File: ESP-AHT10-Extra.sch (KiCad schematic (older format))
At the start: 26 parts, among them J1 USB, SW1 RESET, SW2 PROG, U1 CH330N, U2 HT7233, U3 ESP-12, U4 AHT10, U5 USBLC6-2SC6

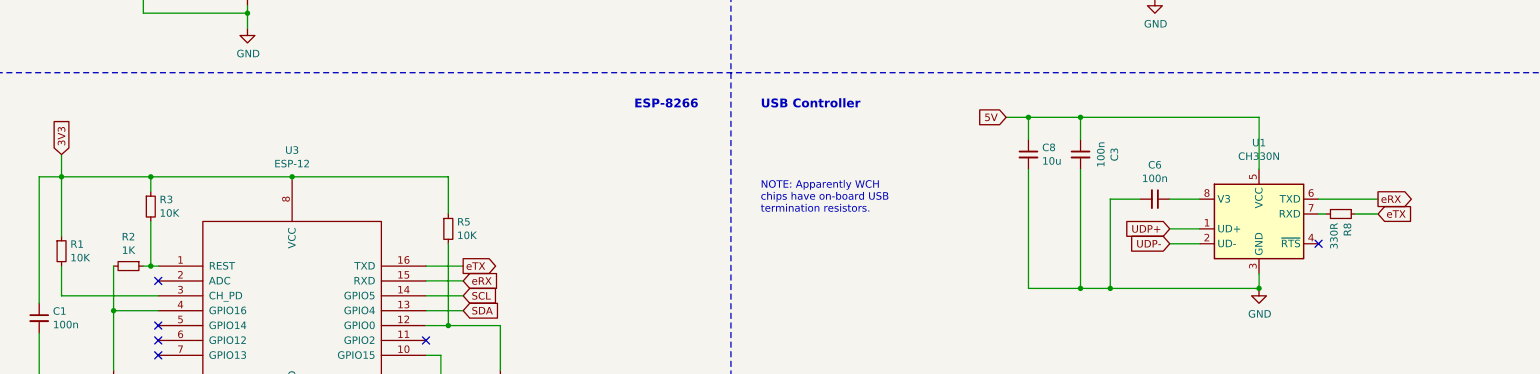
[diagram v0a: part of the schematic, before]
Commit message: really no excuse not to connect RTS to RESET
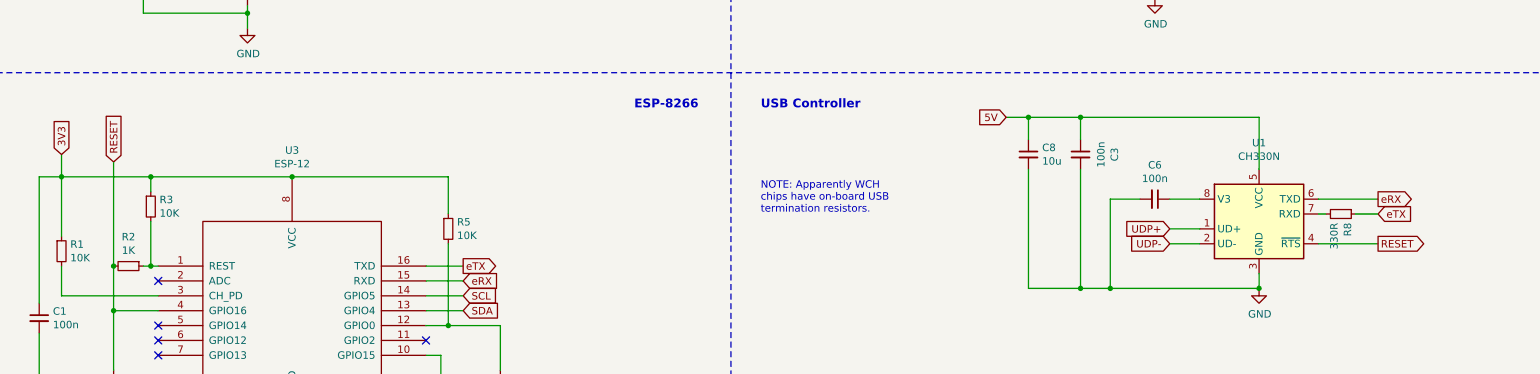
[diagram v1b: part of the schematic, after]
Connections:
- net RESET: now reaches R2.2, SW1.1, U3.4 (GPIO16)
- net RESET: now also U1.4 (~RTS)
- no-connect marks 6 -> 5
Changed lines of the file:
@@
 Wire Wire Line
 	8550 5750 8750 5750
-NoConn ~ 9550 5750
 $Comp
 L power:GND #PWR01
@@
 Text Notes 650  7600 0    50   ~ 0
 NOTE: R3 isn't needed for\nESP modules having an internal\nRESET pull-up. It'll still work if you\nadd it though.
+Text GLabel 1450 5200 1    50   Input ~ 0
+RESET
+Wire Wire Line
+	1450 5200 1450 5900
+Connection ~ 1450 5900
+Text GLabel 9950 5750 2    50   Output ~ 0
+RESET
+Wire Wire Line
+	9550 5750 9950 5750
 $EndSCHEMATC

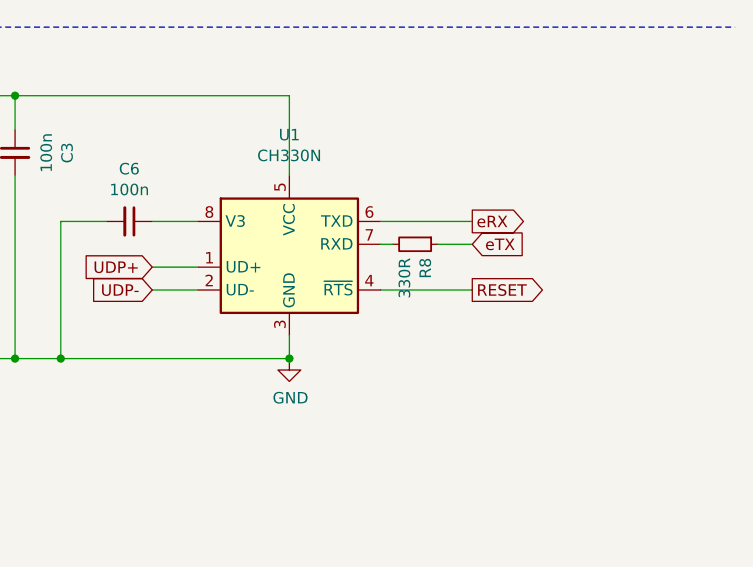
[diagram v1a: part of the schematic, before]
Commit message: fix R8's value
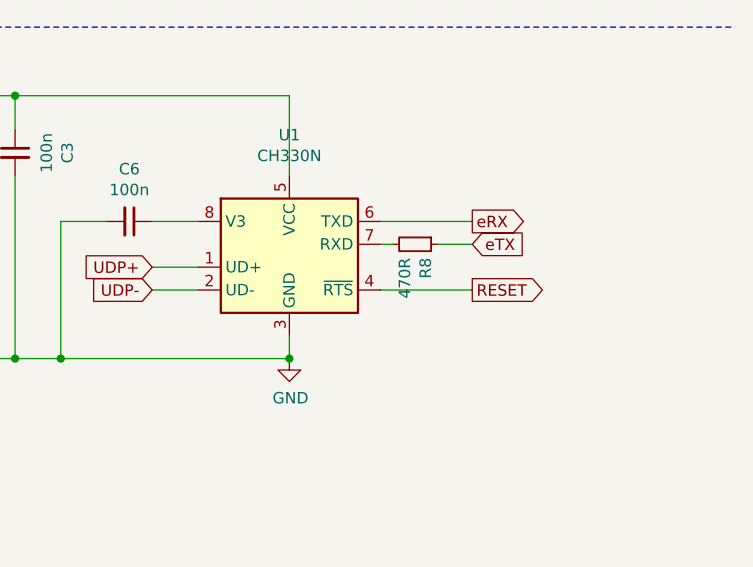
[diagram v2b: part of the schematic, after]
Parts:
- R8: value 330R -> 470R
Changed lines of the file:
@@
 P 9700 5550
 F 0 "R8" H 9759 5596 50  0000 L CNN
-F 1 "330R" H 9759 5505 50  0000 L CNN
+F 1 "470R" H 9759 5505 50  0000 L CNN
 F 2 "Resistors_SMD:R_0805" H 9700 5550 50  0001 C CNN
 F 3 "~" H 9700 5550 50  0001 C CNN

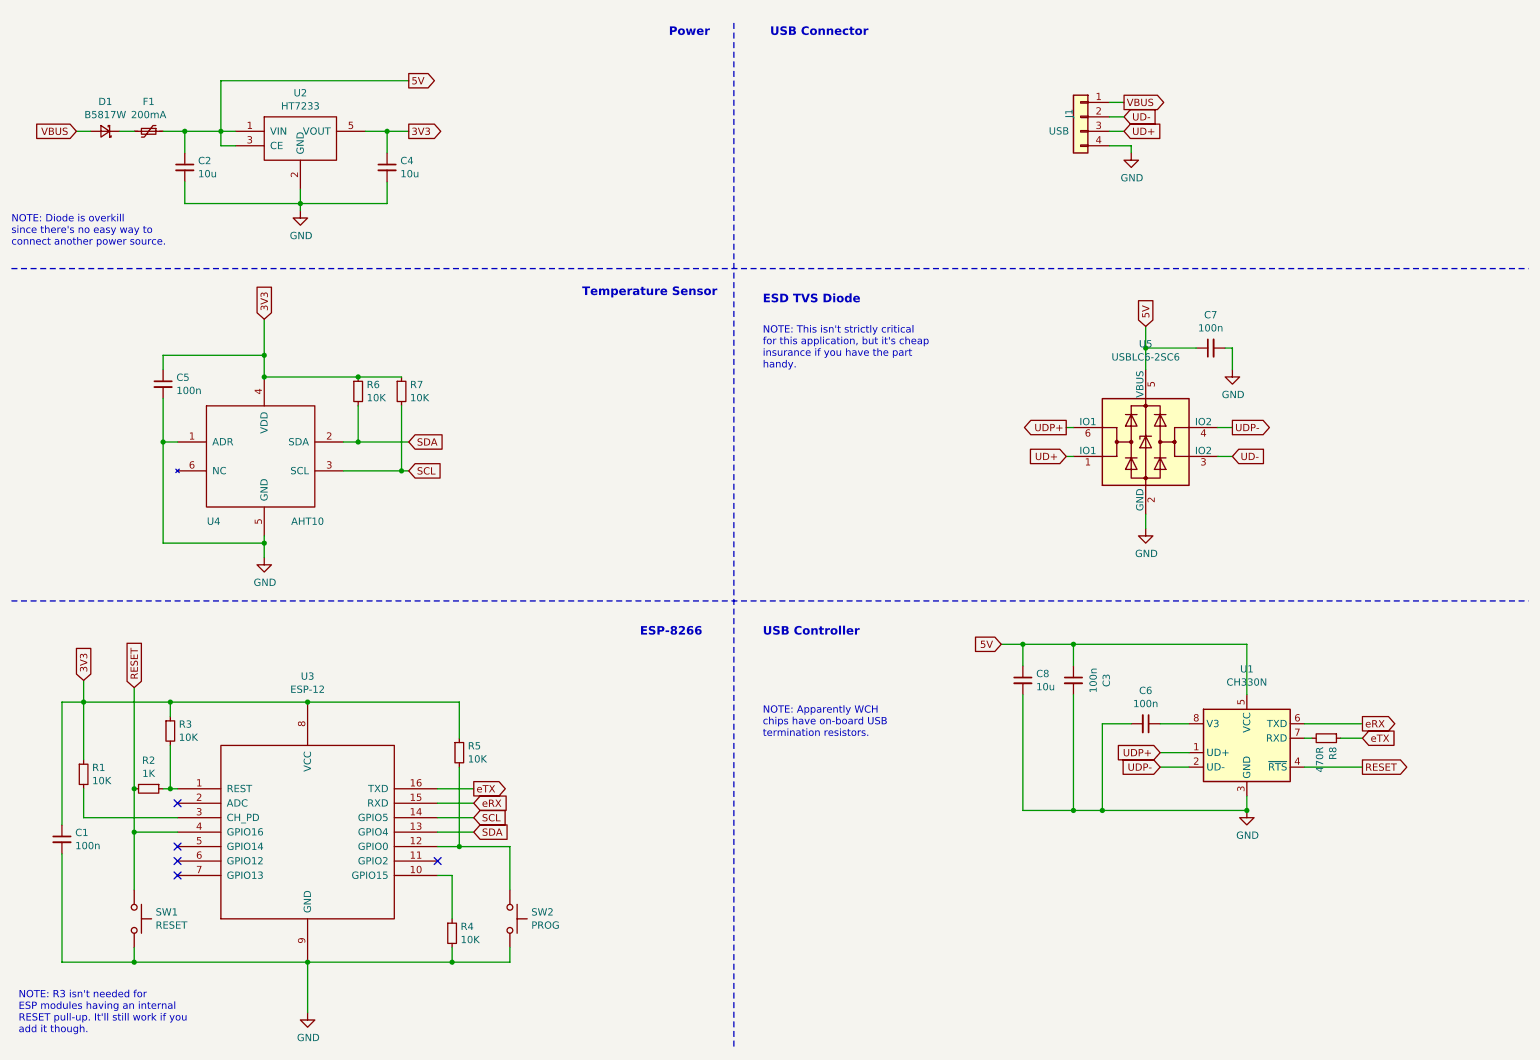
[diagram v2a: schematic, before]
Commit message: try adding a WLED.
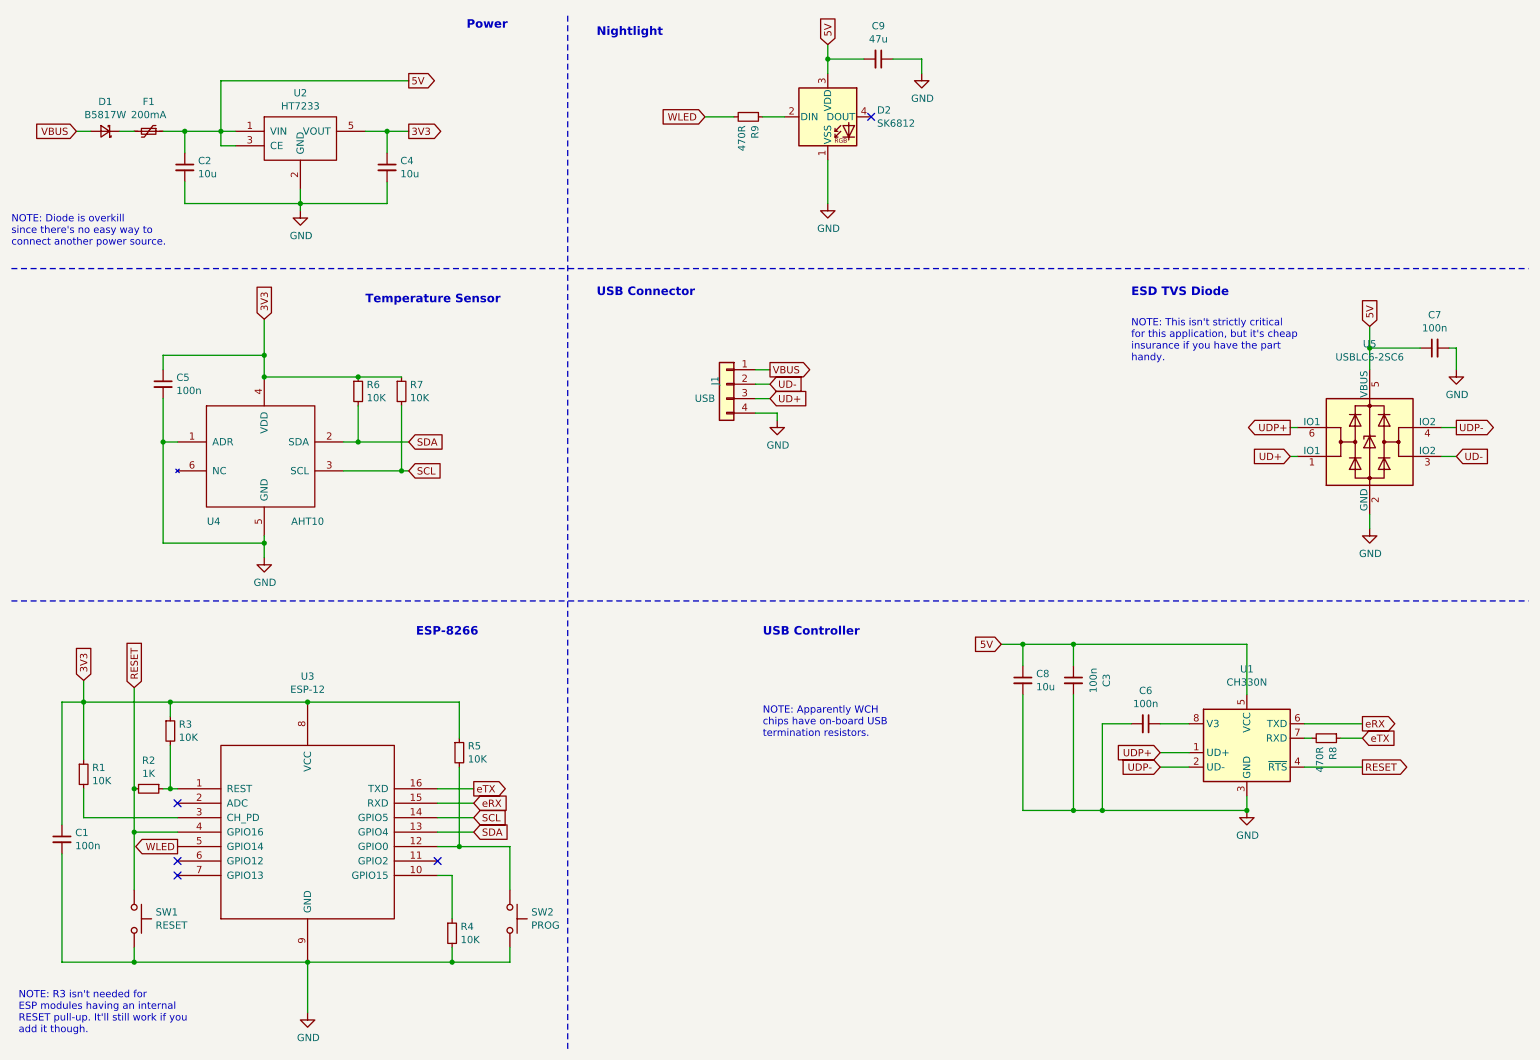
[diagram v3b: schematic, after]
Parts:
- added C9: 47u, symbol Device:C_Small
- added D2: SK6812, LED_SMD:LED_SK6812_PLCC4_5.0x5.0mm_P3.2mm, symbol LED:SK6812
- added R9: 470R, Resistors_SMD:R_0805, symbol Device:R_Small
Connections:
- net 5V: now also C9.2, D2.3 (VDD)
- net GND: now also C9.1, D2.1 (VSS)
- net WLED: now reaches U3.5 (GPIO14)
- net WLED: now also R9.2
- new net: D2.2 (DIN), R9.1
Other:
- note added: "Nightlight"
- moved on the sheet: C7, J1, U5
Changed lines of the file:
@@
 L Connector_Generic:Conn_01x04 J1
 U 1 1 5DBDB3F6
-P 8000 1250
-F 0 "J1" V 8080 1242 50  0000 L CNN
-F 1 "USB" H 8080 1151 50  0000 L CNN
-F 2 "CPB:usb-PCB" H 8000 1250 50  0001 C CNN
-F 3 "~" H 8000 1250 50  0001 C CNN
-	1    8000 1250
+P 5550 3100
+F 0 "J1" V 5630 3092 50  0000 L CNN
+F 1 "USB" H 5630 3001 50  0000 L CNN
+F 2 "CPB:usb-PCB" H 5550 3100 50  0001 C CNN
+F 3 "~" H 5550 3100 50  0001 C CNN
+	1    5550 3100
 	-1   0    0    -1
 $EndComp
@@
 	1450 6200 1750 6200
 NoConn ~ 1750 6000
-NoConn ~ 1750 6300
 NoConn ~ 1750 6400
 NoConn ~ 1750 6500
@@
 	1    0    0    -1
 $EndComp
-Text GLabel 8300 1250 2    50   Input ~ 0
+Text GLabel 5850 3100 2    50   Input ~ 0
 UD-
-Text GLabel 8300 1350 2    50   Input ~ 0
+Text GLabel 5850 3200 2    50   Input ~ 0
 UD+
-Text GLabel 9050 3600 2    50   Input ~ 0
+Text GLabel 10600 3600 2    50   Input ~ 0
 UD-
-Text GLabel 7900 3600 0    50   Input ~ 0
+Text GLabel 9450 3600 0    50   Input ~ 0
 UD+
 Wire Wire Line
@@
 L Power_Protection:USBLC6-2SC6 U5
 U 1 1 5DC39FB1
-P 8450 3500
-F 0 "U5" H 8450 4178 50  0000 C CNN
-F 1 "USBLC6-2SC6" H 8450 4087 50  0000 C CNN
-F 2 "Package_TO_SOT_SMD:SOT-23-6" H 7700 3900 50  0001 C CNN
-F 3 "http://www2.st.com/resource/en/datasheet/CD00050750.pdf" H 8650 3850 50  0001 C CNN
-	1    8450 3500
+P 10000 3500
+F 0 "U5" H 10000 4178 50  0000 C CNN
+F 1 "USBLC6-2SC6" H 10000 4087 50  0000 C CNN
+F 2 "Package_TO_SOT_SMD:SOT-23-6" H 9250 3900 50  0001 C CNN
+F 3 "http://www2.st.com/resource/en/datasheet/CD00050750.pdf" H 10200 3850 50  0001 C CNN
+	1    10000 3500
 	1    0    0    -1
 $EndComp
@@
 L power:GND #PWR05
 U 1 1 5DC4A8A6
-P 8450 4100
-F 0 "#PWR05" H 8450 3850 50  0001 C CNN
-F 1 "GND" H 8455 3927 50  0000 C CNN
-F 2 "" H 8450 4100 50  0001 C CNN
-F 3 "" H 8450 4100 50  0001 C CNN
-	1    8450 4100
-	1    0    0    -1
-$EndComp
-Text GLabel 7900 3400 0    50   Output ~ 0
+P 10000 4100
+F 0 "#PWR05" H 10000 3850 50  0001 C CNN
+F 1 "GND" H 10005 3927 50  0000 C CNN
+F 2 "" H 10000 4100 50  0001 C CNN
+F 3 "" H 10000 4100 50  0001 C CNN
+	1    10000 4100
+	1    0    0    -1
+$EndComp
+Text GLabel 9450 3400 0    50   Output ~ 0
 UDP+
-Text GLabel 9050 3400 2    50   Output ~ 0
+Text GLabel 10600 3400 2    50   Output ~ 0
 UDP-
 Wire Wire Line
-	7900 3400 7950 3400
-Wire Wire Line
-	7900 3600 7950 3600
-Wire Wire Line
-	8950 3400 9050 3400
-Wire Wire Line
-	8950 3600 9050 3600
-Wire Wire Line
-	8450 4000 8450 4100
+	9450 3400 9500 3400
+Wire Wire Line
+	9450 3600 9500 3600
+Wire Wire Line
+	10500 3400 10600 3400
+Wire Wire Line
+	10500 3600 10600 3600
+Wire Wire Line
+	10000 4000 10000 4100
 Connection ~ 1800 1350
 $Comp
@@
 L power:GND #PWR0101
 U 1 1 5DC645A4
-P 8350 1500
-F 0 "#PWR0101" H 8350 1250 50  0001 C CNN
-F 1 "GND" H 8355 1327 50  0000 C CNN
-F 2 "" H 8350 1500 50  0001 C CNN
-F 3 "" H 8350 1500 50  0001 C CNN
-	1    8350 1500
-	1    0    0    -1
-$EndComp
-Text GLabel 8300 1150 2    50   Output ~ 0
+P 5900 3350
+F 0 "#PWR0101" H 5900 3100 50  0001 C CNN
+F 1 "GND" H 5905 3177 50  0000 C CNN
+F 2 "" H 5900 3350 50  0001 C CNN
+F 3 "" H 5900 3350 50  0001 C CNN
+	1    5900 3350
+	1    0    0    -1
+$EndComp
+Text GLabel 5850 3000 2    50   Output ~ 0
 VBUS
 Text GLabel 1050 1350 0    50   Input ~ 0
 VBUS
 Wire Wire Line
-	8200 1150 8300 1150
-Wire Wire Line
-	8200 1250 8300 1250
-Wire Wire Line
-	8200 1350 8300 1350
-Wire Wire Line
-	8200 1450 8350 1450
-Wire Wire Line
-	8350 1450 8350 1500
+	5750 3000 5850 3000
+Wire Wire Line
+	5750 3100 5850 3100
+Wire Wire Line
+	5750 3200 5850 3200
+Wire Wire Line
+	5750 3300 5900 3300
+Wire Wire Line
+	5900 3300 5900 3350
 Text GLabel 3350 1000 2    50   Output ~ 0
 5V
@@
 L Device:C_Small C7
 U 1 1 5DC83A5A
-P 8900 2850
-F 0 "C7" V 8671 2850 50  0000 C CNN
-F 1 "100n" V 8762 2850 50  0000 C CNN
-F 2 "Capacitors_SMD:C_0805" H 8900 2850 50  0001 C CNN
-F 3 "~" H 8900 2850 50  0001 C CNN
-	1    8900 2850
+P 10450 2850
+F 0 "C7" V 10221 2850 50  0000 C CNN
+F 1 "100n" V 10312 2850 50  0000 C CNN
+F 2 "Capacitors_SMD:C_0805" H 10450 2850 50  0001 C CNN
+F 3 "~" H 10450 2850 50  0001 C CNN
+	1    10450 2850
 	0    -1   1    0
 $EndComp
 Wire Wire Line
-	8450 2700 8450 2850
-Wire Wire Line
-	8450 2850 8800 2850
-Connection ~ 8450 2850
-Wire Wire Line
-	8450 2850 8450 3000
+	10000 2700 10000 2850
+Wire Wire Line
+	10000 2850 10350 2850
+Connection ~ 10000 2850
+Wire Wire Line
+	10000 2850 10000 3000
 $Comp
 L power:GND #PWR06
 U 1 1 5DC88A59
-P 9050 3000
-F 0 "#PWR06" H 9050 2750 50  0001 C CNN
-F 1 "GND" H 9055 2827 50  0000 C CNN
-F 2 "" H 9050 3000 50  0001 C CNN
-F 3 "" H 9050 3000 50  0001 C CNN
-	1    9050 3000
-	1    0    0    -1
-$EndComp
-Wire Wire Line
-	9000 2850 9050 2850
-Wire Wire Line
-	9050 2850 9050 3000
+P 10600 3000
+F 0 "#PWR06" H 10600 2750 50  0001 C CNN
+F 1 "GND" H 10605 2827 50  0000 C CNN
+F 2 "" H 10600 3000 50  0001 C CNN
+F 3 "" H 10600 3000 50  0001 C CNN
+	1    10600 3000
+	1    0    0    -1
+$EndComp
+Wire Wire Line
+	10550 2850 10600 2850
+Wire Wire Line
+	10600 2850 10600 3000
 Text Notes 5800 5550 0    50   ~ 0
 NOTE: Apparently WCH\nchips have on-board USB\ntermination resistors.
@@
 Wire Wire Line
 	1350 1350 1450 1350
-Text GLabel 8450 2700 1    50   Input ~ 0
+Text GLabel 10000 2700 1    50   Input ~ 0
 5V
 Wire Wire Line
@@
 Wire Wire Line
 	2050 1000 3350 1000
-Text Notes 5850 700  0    59   ~ 12
+Text Notes 4650 2500 0    59   ~ 12
 USB Connector
-Text Notes 5150 700  0    59   ~ 12
+Text Notes 3750 650  0    59   ~ 12
 Power
-Text Notes 5800 2550 0    59   ~ 12
+Text Notes 8350 2500 0    59   ~ 12
 ESD TVS Diode
 Text Notes 5800 4850 0    59   ~ 12
 USB Controller
-Text Notes 4550 2500 0    59   ~ 12
+Text Notes 3050 2550 0    59   ~ 12
 Temperature Sensor
-Text Notes 4950 4850 0    59   ~ 12
+Text Notes 3400 4850 0    59   ~ 12
 ESP-8266
 Wire Notes Line
@@
 Wire Notes Line
 	600  4600 11100 4600
-Wire Notes Line
-	5600 600  5600 7700
-Text Notes 5800 3000 0    50   ~ 0
+Text Notes 8350 2950 0    50   ~ 0
 NOTE: This isn't strictly critical\nfor this application, but it's cheap\ninsurance if you have the part\nhandy.
 Text Notes 600  2150 0    50   ~ 0
@@
 Wire Wire Line
 	9550 5750 9950 5750
+Wire Notes Line
+	4450 7700 4450 550
+$Comp
+L LED:SK6812 D2
+U 1 1 5DD551FE
+P 6250 1250
+F 0 "D2" H 6591 1296 50  0000 L CNN
+F 1 "SK6812" H 6591 1205 50  0000 L CNN
+F 2 "LED_SMD:LED_SK6812_PLCC4_5.0x5.0mm_P3.2mm" H 6300 950 50  0001 L TNN
+F 3 "https://cdn-shop.adafruit.com/product-files/1138/SK6812+LED+datasheet+.pdf" H 6350 875 50  0001 L TNN
+	1    6250 1250
+	1    0    0    -1
+$EndComp
+Text GLabel 1750 6300 0    50   Output ~ 0
+WLED
+Text GLabel 5400 1250 0    50   Input ~ 0
+WLED
+$Comp
+L Device:R_Small R9
+U 1 1 5DD55710
+P 5700 1250
+F 0 "R9" H 5759 1296 50  0000 L CNN
+F 1 "470R" H 5759 1205 50  0000 L CNN
+F 2 "Resistors_SMD:R_0805" H 5700 1250 50  0001 C CNN
+F 3 "~" H 5700 1250 50  0001 C CNN
+	1    5700 1250
+	0    1    1    0
+$EndComp
+Text GLabel 6250 750  1    50   Input ~ 0
+5V
+$Comp
+L power:GND #PWR07
+U 1 1 5DD58857
+P 6250 1850
+F 0 "#PWR07" H 6250 1600 50  0001 C CNN
+F 1 "GND" H 6255 1677 50  0000 C CNN
+F 2 "" H 6250 1850 50  0001 C CNN
+F 3 "" H 6250 1850 50  0001 C CNN
+	1    6250 1850
+	1    0    0    -1
+$EndComp
+NoConn ~ 6550 1250
+$Comp
+L Device:C_Small C9
+U 1 1 5DD5E86C
+P 6600 850
+F 0 "C9" V 6371 850 50  0000 C CNN
+F 1 "47u" V 6462 850 50  0000 C CNN
+F 2 "" H 6600 850 50  0001 C CNN
+F 3 "~" H 6600 850 50  0001 C CNN
+	1    6600 850
+	0    1    1    0
+$EndComp
+Wire Wire Line
+	5400 1250 5600 1250
+Wire Wire Line
+	5800 1250 5950 1250
+Wire Wire Line
+	6250 750  6250 850
+Wire Wire Line
+	6250 1550 6250 1850
+$Comp
+L power:GND #PWR08
+U 1 1 5DD6B19B
+P 6900 950
+F 0 "#PWR08" H 6900 700 50  0001 C CNN
+F 1 "GND" H 6905 777 50  0000 C CNN
+F 2 "" H 6900 950 50  0001 C CNN
+F 3 "" H 6900 950 50  0001 C CNN
+	1    6900 950
+	1    0    0    -1
+$EndComp
+Wire Wire Line
+	6250 850  6500 850
+Connection ~ 6250 850
+Wire Wire Line
+	6250 850  6250 950
+Wire Wire Line
+	6700 850  6900 850
+Wire Wire Line
+	6900 850  6900 950
+Text Notes 4650 700  0    59   ~ 12
+Nightlight
 $EndSCHEMATC
